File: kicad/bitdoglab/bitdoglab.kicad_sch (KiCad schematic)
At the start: 56 parts, among them J1 Conn_01x20_Socket, J10 3V3, J11 5V-VSYS, J12 Conn_01x05_Pin, J13 Conn_01x05_Pin, J14 5x5 Matrix led, J15 0, J16 1, J17 2, J18 3, J19 JOYSTICK, J2 conector_idc, J20 Conn_01x04_Pin, J21 Conn_01x04_Pin, J22 Conn_01x04_Pin, J3 Conn_01x20_Socket, J4 jumper_mic, J5 Conn_01x05_Pin, J6 Conn_01x05_Pin, J7 GND, J8 ANA-IN, J9 GND, Q1 DMG2305UX-13, Q2 BC337, Q3 BC337, SW1 Reset, SW2 Botão, SW3 Button_B, U1 3.3v_tht, U4 MIC

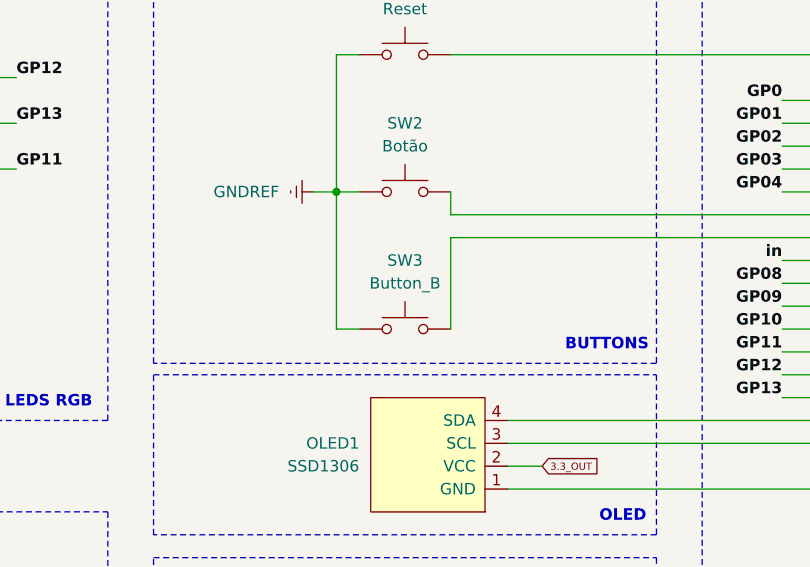
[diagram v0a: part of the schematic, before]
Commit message: change buttons footprints for 12mm
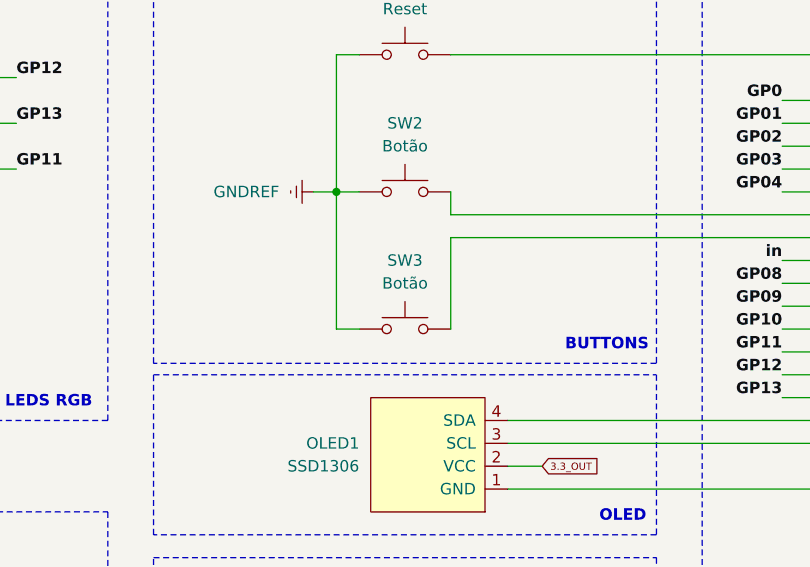
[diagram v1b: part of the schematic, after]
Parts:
- SW2: footprint Button_Switch_THT:SW_PUSH_6mm -> Button_Switch_THT:SW_PUSH-12mm
- SW3: value Button_B -> Botão; footprint Button_Switch_THT:SW_PUSH_6mm -> Button_Switch_THT:SW_PUSH-12mm
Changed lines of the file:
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@@
 			)
 		)
-		(property "Footprint" "Button_Switch_THT:SW_PUSH_6mm"
+		(property "Footprint" "Button_Switch_THT:SW_PUSH-12mm"
 			(at 111.76 86.36 0)
 			(effects
@@
 			)
 		)
-		(property "Value" "Button_B"
+		(property "Value" "Botão"
 			(at 111.76 101.6 0)
 			(effects
@@
 			)
 		)
-		(property "Footprint" "Button_Switch_THT:SW_PUSH_6mm"
+		(property "Footprint" "Button_Switch_THT:SW_PUSH-12mm"
 			(at 111.76 101.6 0)
 			(effects
